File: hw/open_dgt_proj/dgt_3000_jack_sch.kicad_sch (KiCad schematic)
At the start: 4 parts, among them J1 AudioPlug3, J2 YXF29886, U2 STM8L152M8

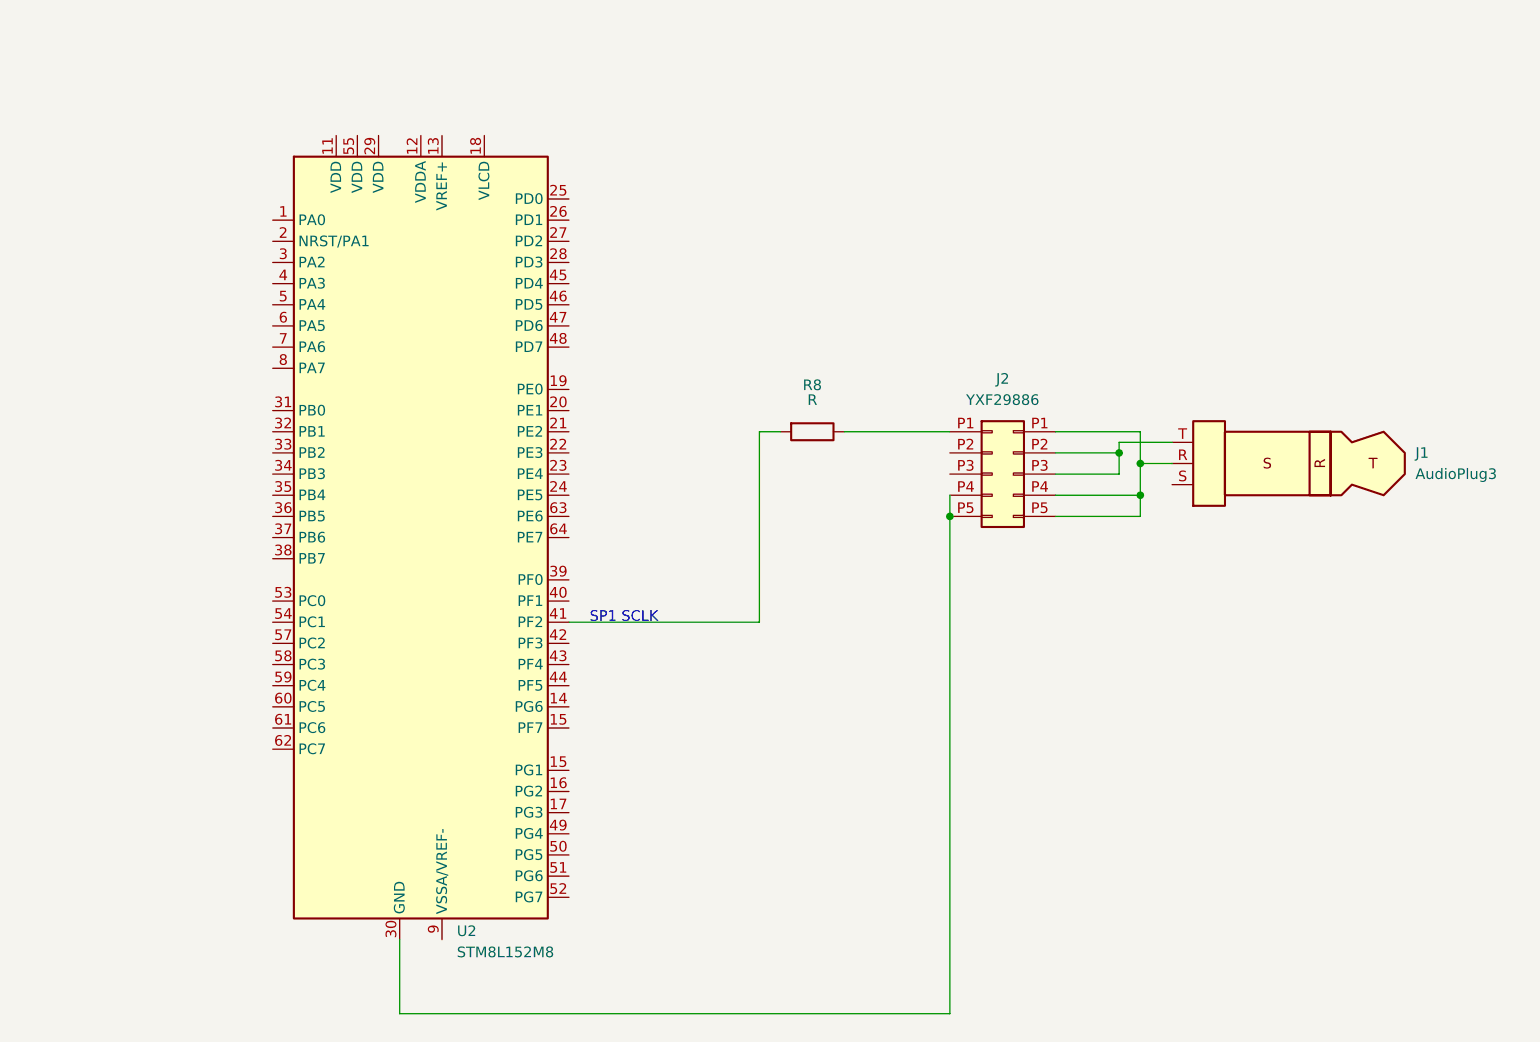
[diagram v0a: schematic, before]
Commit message: Updated schematic for DGT3000 clock
Signed-off-by: MN3141 <mihai.neag@ulbsibiu.ro>
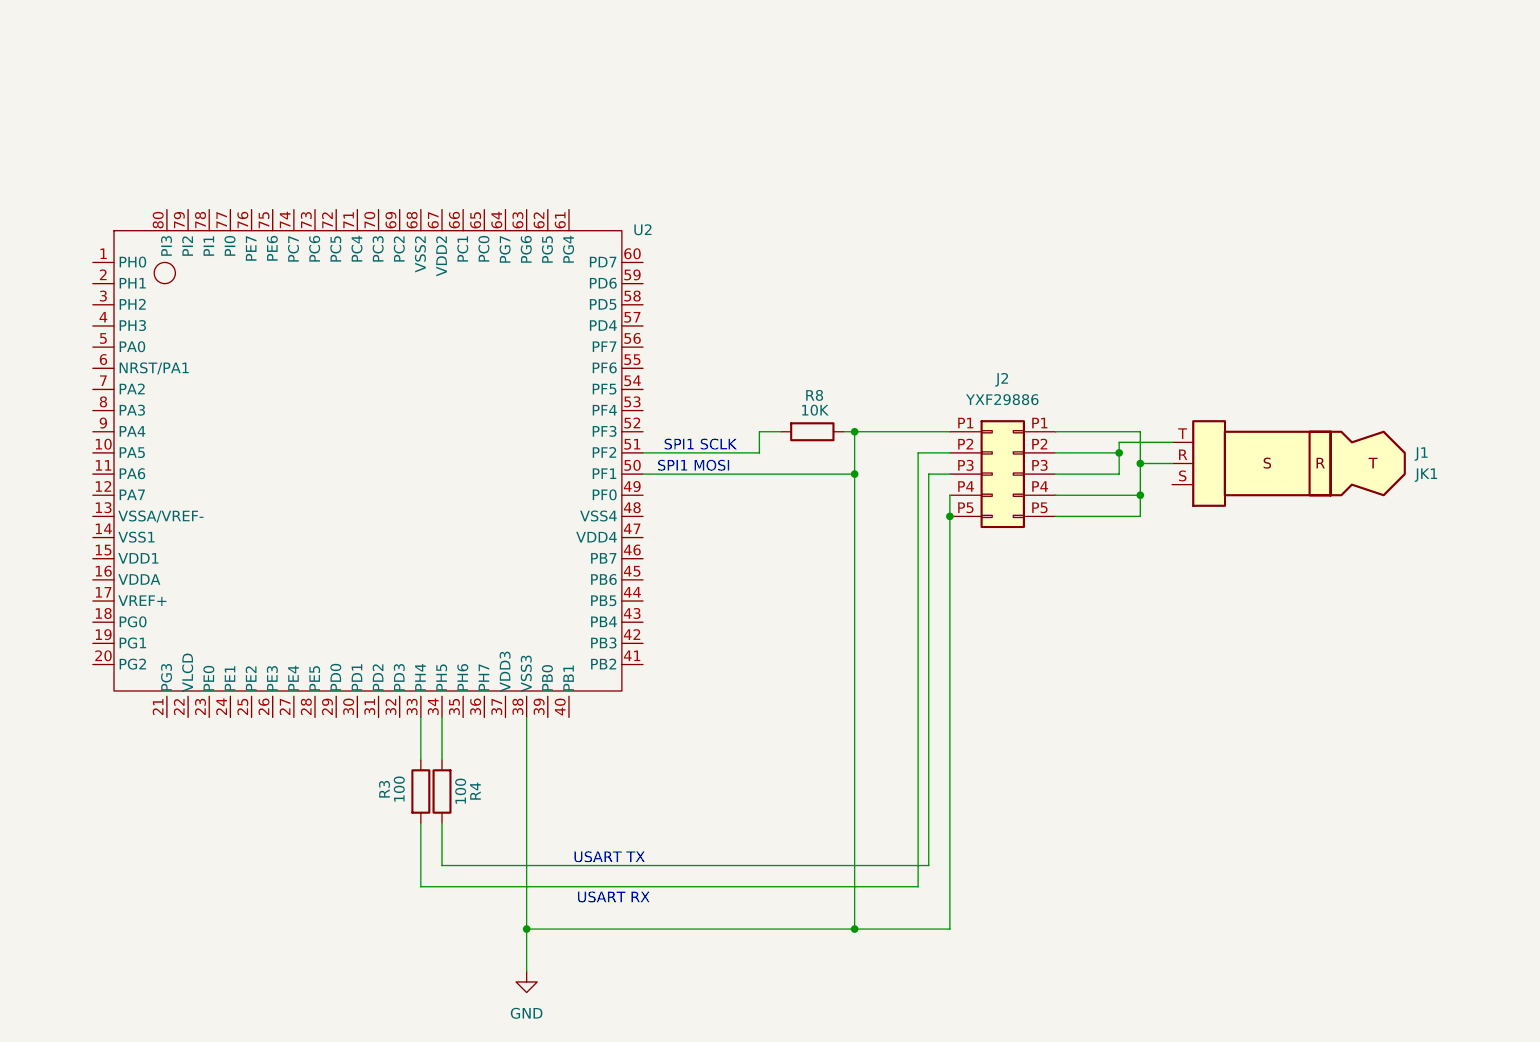
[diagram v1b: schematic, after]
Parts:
- removed U2: STM8L152M8, Package_QFP:LQFP-64_10x10mm_P0.5mm, symbol MCU_ST_STM8:STM8L152R8T
- added R3, R4: 100, symbol Device:R
- added U2: (no value), symbol OpenDGT:STM8L152M8
- J1: value AudioPlug3 -> JK1
- R8: value R -> 10K
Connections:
- net GND: now reaches J2.P4 (Pin4_Jack), J2.P5 (Pin5_Jack)
- net GND: now also J2.P1 (Pin1_Jack), R8.1, U2.38 (VSS3), U2.50 (PF1)
- net at R8.2: now also U2.51 (PF2)
- net at J2.P2 (Pin2_Jack\): now also R3.2
- new net: J2.P3 (Pin3_Jack), R4.1
- new net: R4.2, U2.34 (PH5)
- new net: R3.1, U2.33 (PH4)
- new net: J1.R, J2.P1 (Pin1_Jack), J2.P4 (Pin4_Jack), J2.P5 (Pin5_Jack)
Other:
- note added: "SPI1 MOSI"
- note added: "SPI1 SCLK"
- note added: "USART RX"
- note added: "USART TX"
- note removed: "SP1 SCLK"

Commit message: Added the rest of Jack connections (#30)
Signed-off-by: MN3141 <mihai.neag@ulbsibiu.ro>
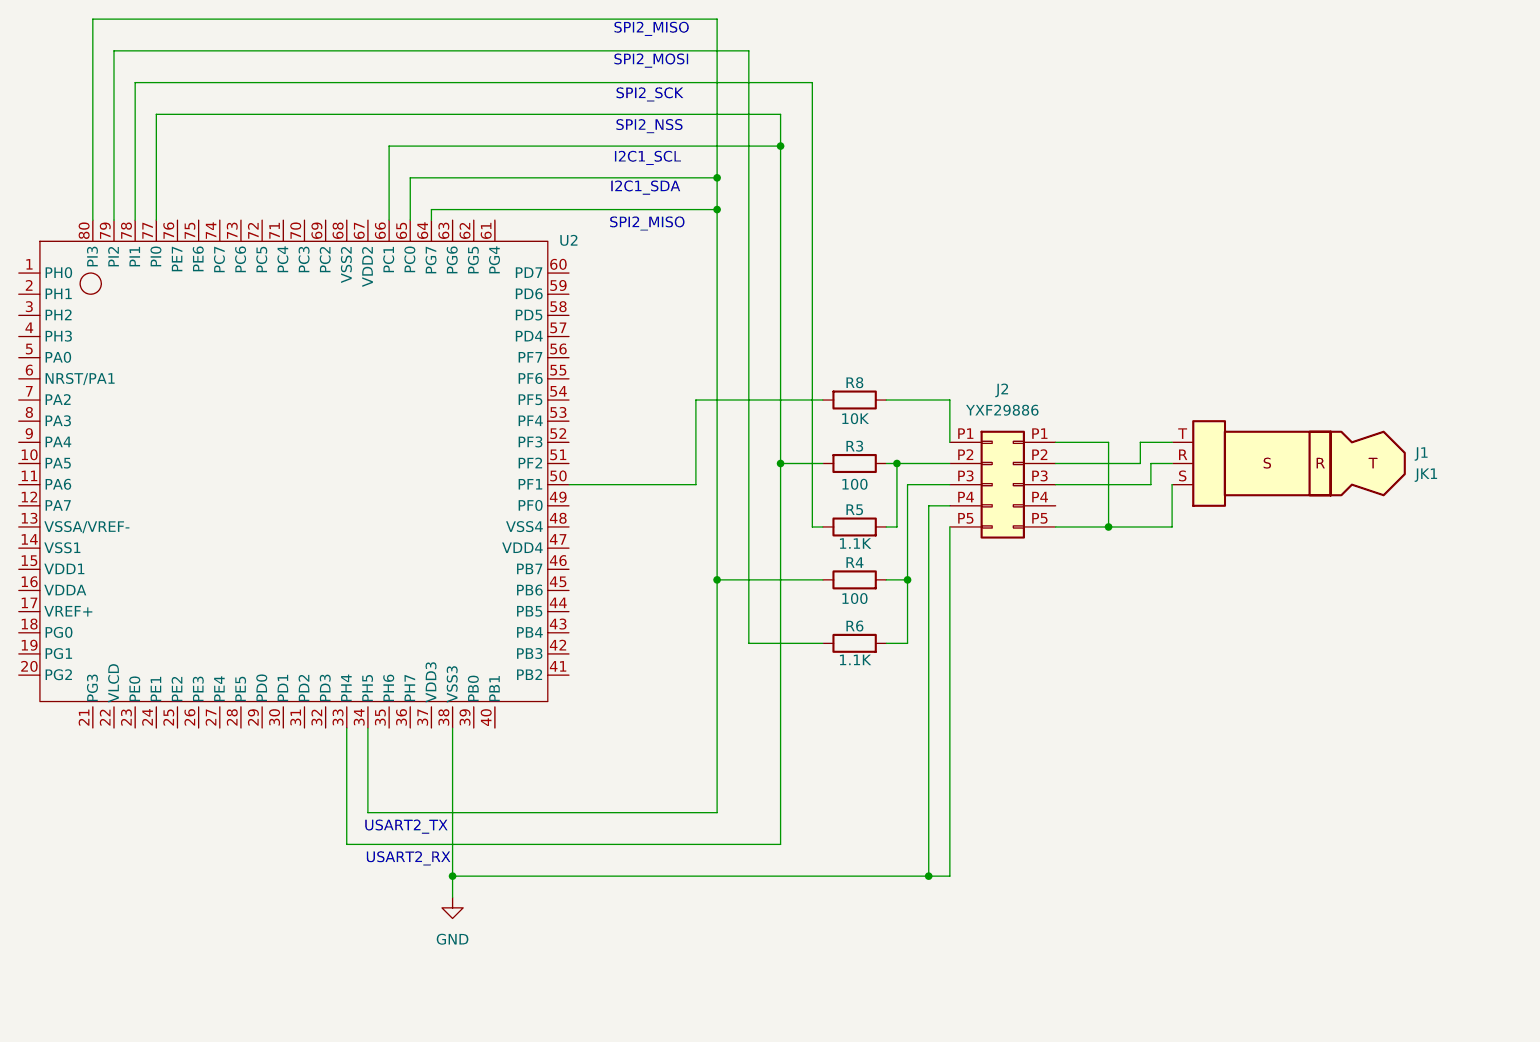
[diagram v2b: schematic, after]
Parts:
- added R5, R6: 1.1K, symbol Device:R
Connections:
- net GND: no longer J2.P1 (Pin1_Jack), R8.1, U2.50 (PF1)
- net at R4.1: now also U2.34 (PH5), U2.64 (PG7), U2.65 (PC0), U2.80 (PI3); no longer J2.P3 (Pin3_Jack)
- net at R4.2: now also J2.P3 (Pin3_Jack), R6.2; no longer U2.34 (PH5)
- net at R3.1: now also J2.P2 (Pin2_Jack\), R5.2; no longer U2.33 (PH4)
- net at R8.2: now also U2.50 (PF1); no longer U2.51 (PF2)
- net at U2.66 (PC1): now also R3.2, U2.33 (PH4), U2.77 (PI0)
- net at U2.78 (PI1): now also R5.1
- net at U2.79 (PI2): now also R6.1
- net at J1.T, J2.P2 (Pin2_Jack\): no longer J2.P3 (Pin3_Jack)
- net at J1.S: now also J2.P1 (Pin1_Jack), J2.P5 (Pin5_Jack)
- new net: J2.P1 (Pin1_Jack), R8.1
- new net: J1.R, J2.P3 (Pin3_Jack)
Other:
- note added: "I2C1_SCL"
- note added: "I2C1_SDA"
- note added: "SPI2_MISO"
- note added: "SPI2_MOSI"
- note added: "SPI2_NSS"
- note added: "SPI2_SCK"
- note added: "USART2_RX"
- note added: "USART2_TX"
- note removed: "SPI1 MOSI"
- note removed: "SPI1 SCLK"
- note removed: "USART RX"
- note removed: "USART TX"
- moved on the sheet: J2, R3, R4, R8, U2
